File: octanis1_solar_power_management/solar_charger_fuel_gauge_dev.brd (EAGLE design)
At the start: 95 x 43.4 mm, 98 parts, among them IC401 TUSB2046BIRHBIRHB, Q2 32.768kHz, Q4 CSTCR4M00G15L99, Q401 CSTCR6M00G15L99, T1 BC547, U1 BQ24210, U2 BQ27510_DRZ_12, U3 TPS61240DRVT, U402 TPS62237DRY, U404 TPD2E001DRLR, U6 MSP430F5529IPNR

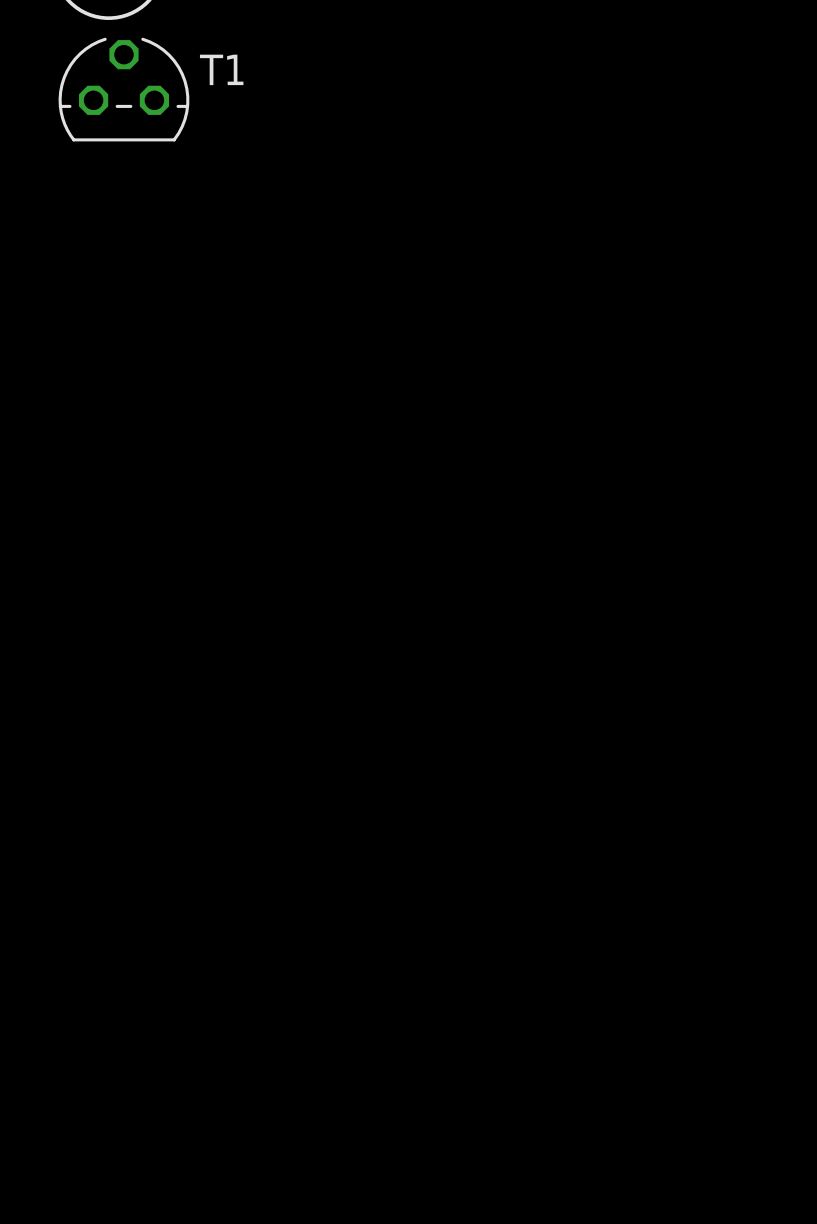
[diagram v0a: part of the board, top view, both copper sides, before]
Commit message: added heating circuit
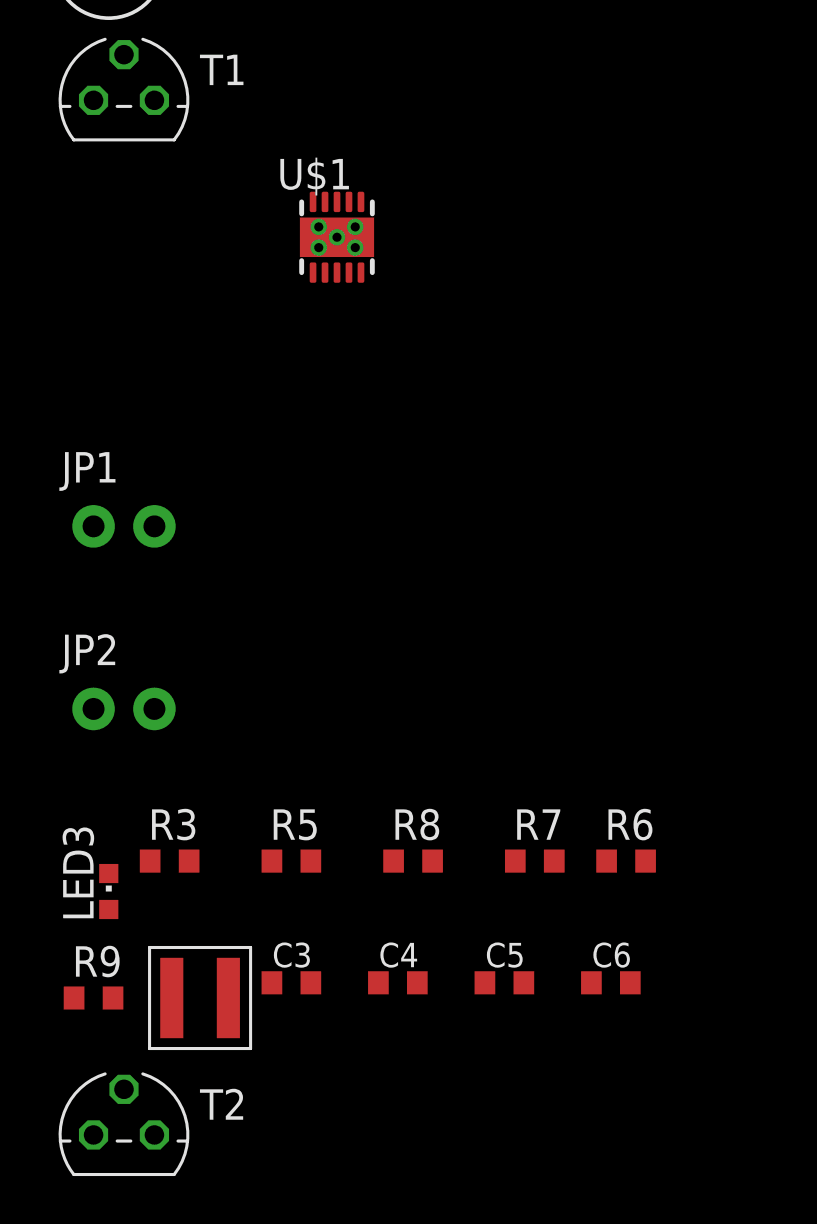
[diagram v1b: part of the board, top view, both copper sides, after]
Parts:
- added C3, C5, C6: 22uF, adafruit:C0603K
- added C4: 10nF, adafruit:C0603K
- added JP1, JP2: M021X02_NO_SILK, SparkFun-Connectors:1X02_NO_SILK
- added L1: 1uH, Coilcraft:XFL4020
- added LED3: (no value), adafruit:CHIPLED_0603
- added R3: 402k, adafruit:R0603
- added R5: 100k, adafruit:R0603
- added R6: 1k, adafruit:R0603
- added R7: 1M, adafruit:R0603
- added R8: 499k, adafruit:R0603
- added R9: 0, adafruit:R0603
- added T2: BC547, transistor:TO92
- added U$1: TPS61230, texas:DRC-S-PVSON-N11
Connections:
- removed net +3V3: C14.1, C19.2, C30.+, HEAT-PAD.2, R27.2, R28.2, RPUC.2, RPUD.2, S5.1, U6.18, U6.50
- removed net N$13: C1.1, SOLAR.2, U1.1
- removed net N$39: T1.1
- removed net N$40: T1.2
- removed net SOLAR: C1.2, R4.1, SOLAR.1, U1.3
- new net IND: L1.P$2, U$1.1, U$1.2
- new net N$42: C4.1, U$1.6
- new net N$43: R3.1, R5.2, U$1.7
- new net N$44: LED3.C, R6.2
- new net N$45: U$1.9
- new net N$46: R8.1, R9.2, U$1.8
- new net N$47: R7.1, R8.2
- new net PG: U$1.5
- new net SOLAR+: C1.1, C14.1, C19.2, C30.+, R27.2, R28.2, RPUC.2, RPUD.2, S5.1, SOLAR.2, T1.3, U1.1, U6.18, U6.50
- new net VIN: C3.1, L1.P$1, R7.2, U$1.10
- new net VOUT: C5.1, C6.1, JP1.1, JP2.1, LED3.A, R3.2, U$1.3, U$1.4
- net BAT+: now also T2.3
- net GND: now also C1.2, C3.2, C4.2, C5.2, C6.2, HEAT-PAD.1, JP1.2, JP2.2, R4.1, R5.1, R6.1, R9.1, SOLAR.1, U$1.GND, U$1.GND@1, U$1.GND@2, U$1.GND@3, U$1.GND@4, U$1.GND@5, U1.3
- net N$37: now also HEAT-PAD.2, T1.1, T2.1; no longer HEAT-PAD.1, T1.3
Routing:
- net SOLAR+: track 0.00 -> 29.0 mm
- net N$13: track 29.0 -> 0.00 mm
- net GND: track 11.7 -> 38.4 mm, vias 0 -> 1
- net SOLAR: track 26.7 -> 0.00 mm, vias 1 -> 0

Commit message: added heating circuit. added correct step up converter. rearranged components to top layer. drew bigger power traces.
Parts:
- removed CPIN: 2.2uF, rcl:C0805
- removed CPOUT: 4.7uF, rcl:C0805
- removed HEAT-PAD: (no value), resistor:P0613V
- removed JP1, JP2: M021X02_NO_SILK, SparkFun-Connectors:1X02_NO_SILK
- removed LP: 1uH, eagle-ltspice:L2012C
- removed R7: 1M, adafruit:R0603
- removed R8: 499k, adafruit:R0603
- removed R9: 0, adafruit:R0603
- removed U3: TPS61240DRVT, TPS61240DRVT:SON65P200X200X80-7N
- added HEATPAD: 22-23-2021, con-molex:22-23-2021
- moved C3 200.3 mm to (19.4, 12.8), turned to 90 degrees
- moved C4 199.6 mm to (23.2, 12.1)
- moved T2 197.1 mm to (13.3, 3.17), turned to 270 degrees
- moved L1 196.8 mm to (16.5, 8.54), turned to 270 degrees
- moved C6 194.4 mm to (28.6, 6.99)
- moved LED3 194.2 mm to (28.6, 8.89), turned to 270 degrees
- moved R6 193.7 mm to (28.6, 11.4)
- moved C5 192.6 mm to (28.6, 5.08)
- moved R5 192.3 mm to (24.8, 9.53), turned to 180 degrees
- moved R3 190.3 mm to (24.8, 6.99)
- moved U$1 164.8 mm to (21.0, 8.35)
- moved T1 159.2 mm to (10.3, 8.57), turned to 270 degrees
- moved U6 14.1 mm to (40.6, 28.0)
- moved TEMP2 12.9 mm to (3.61, 39.4)
- moved RG2 9.93 mm to (4.29, 31.8), turned to 180 degrees
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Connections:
- removed net N$41: LP.2, U3.5
- removed net N$45: U$1.9
- removed net N$46: R8.1, R9.2, U$1.8
- removed net N$47: R7.1, R8.2
- removed net VIN: C3.1, L1.P$1, R7.2, U$1.10
- removed net VOUT: C5.1, C6.1, JP1.1, JP2.1, LED3.A, R3.2, U$1.3, U$1.4
- new net EN_BAT_HEAT: T2.2
- new net EN_SOLAR_HEAT: T1.2
- net 5V: now also C5.1, C6.1, LED3.A, R3.2, U$1.3, U$1.4; no longer CPOUT.1, U3.2, U3.3
- net BAT+: now also C3.1, L1.P$1, U$1.10; no longer CPIN.1, LP.1, U3.6
- net EN5V: now also U$1.9; no longer U3.4
- net GND: now also HEATPAD.2; no longer CPIN.2, CPOUT.2, HEAT-PAD.1, JP1.2, JP2.2, R9.1, U3.1
- net N$37: now also HEATPAD.1; no longer HEAT-PAD.2
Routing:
- net BAT+: track 18.6 -> 72.0 mm
- net SOLAR+: track 29.0 -> 46.6 mm
- net N$37: track 0.00 -> 13.7 mm
- net BAT-: track 3.84 -> 9.46 mm
- net IND: track 0.00 -> 4.60 mm
- net GND: track 38.4 -> 34.7 mm
- added copper zone on layer 16, net GND
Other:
- board size 95 x 43.4 mm -> 75 x 47.4 mm

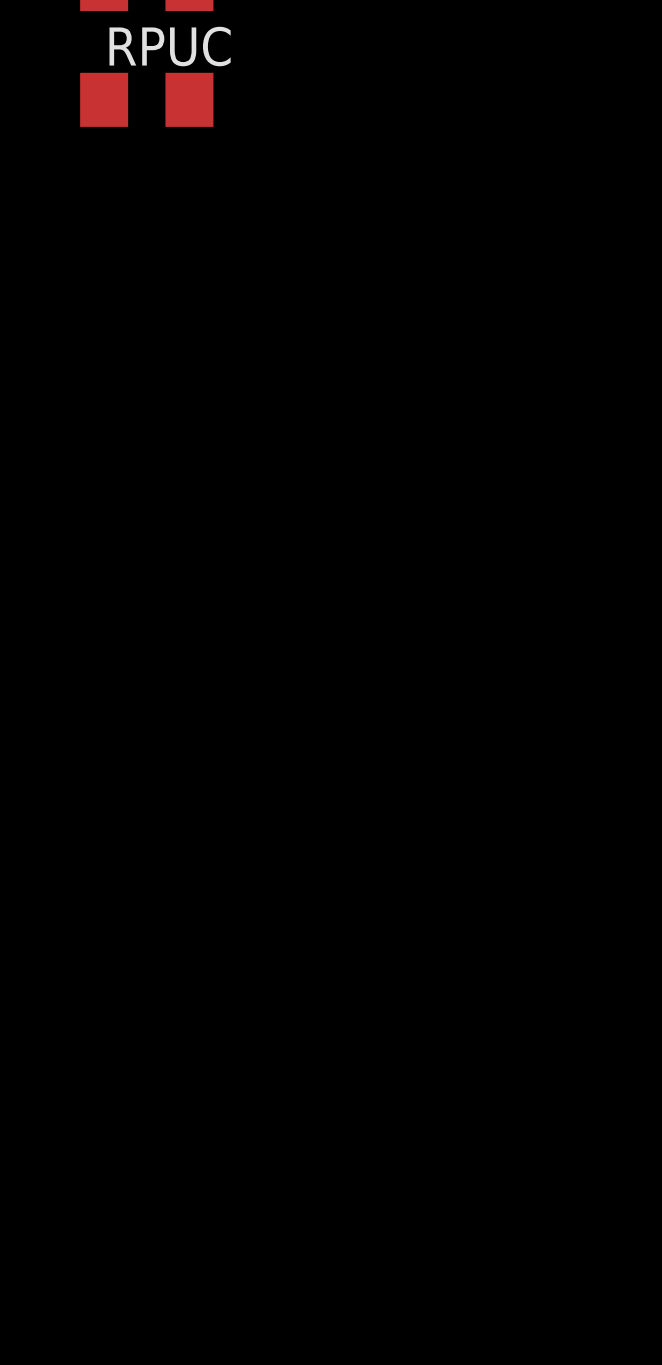
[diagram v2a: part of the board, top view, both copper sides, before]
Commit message: added H-bridge library
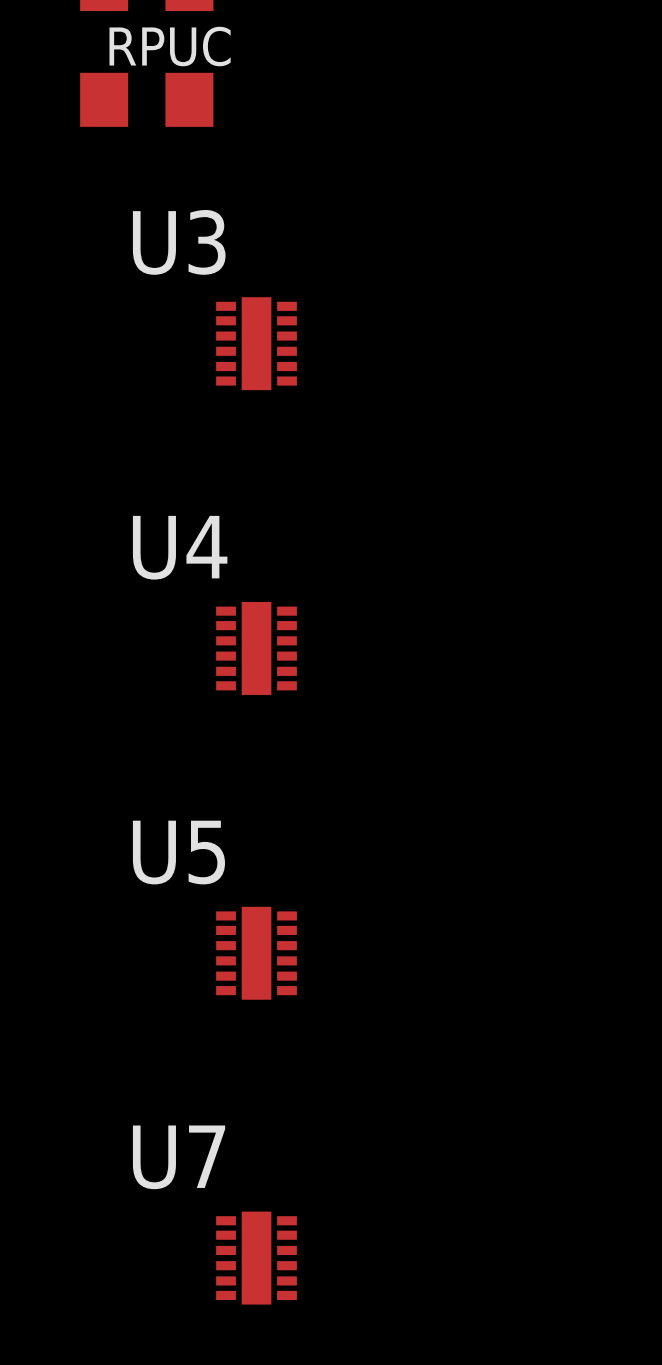
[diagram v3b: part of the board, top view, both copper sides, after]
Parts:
- added U3, U4, U5, U7: DRV8836DSSR, DRV8834:SON50P200X300X80-13N
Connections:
- net BAT+: now also U3.1, U4.1, U5.1, U7.1
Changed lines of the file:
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@@
 <attribute name="OC_FARNELL" value="1462926" x="5.08" y="5.715" size="1.778" layer="27" rot="R90" display="off"/>
+</element>
+<element name="U3" library="DRV8834" package="SON50P200X300X80-13N" value="DRV8836DSSR" x="6.2992" y="-146.9136">
+<attribute name="PACKAGE" value="SON-12" x="6.2992" y="-146.9136" size="1.778" layer="27" display="off"/>
+<attribute name="OC_NEWARK" value="94T6066" x="6.2992" y="-146.9136" size="1.778" layer="27" display="off"/>
+<attribute name="MPN" value="DRV8836DSSR " x="6.2992" y="-146.9136" size="1.778" layer="27" display="off"/>
+<attribute name="SUPPLIER" value="TEXAS INSTRUMENTS" x="6.2992" y="-146.9136" size="1.778" layer="27" display="off"/>
+<attribute name="OC_FARNELL" value="2115236 " x="6.2992" y="-146.9136" size="1.778" layer="27" display="off"/>
+</element>
+<element name="U4" library="DRV8834" package="SON50P200X300X80-13N" value="DRV8836DSSR" x="6.2992" y="-157.0736">
+<attribute name="PACKAGE" value="SON-12" x="6.2992" y="-157.0736" size="1.778" layer="27" display="off"/>
+<attribute name="OC_NEWARK" value="94T6066" x="6.2992" y="-157.0736" size="1.778" layer="27" display="off"/>
+<attribute name="MPN" value="DRV8836DSSR " x="6.2992" y="-157.0736" size="1.778" layer="27" display="off"/>
+<attribute name="SUPPLIER" value="TEXAS INSTRUMENTS" x="6.2992" y="-157.0736" size="1.778" layer="27" display="off"/>
+<attribute name="OC_FARNELL" value="2115236 " x="6.2992" y="-157.0736" size="1.778" layer="27" display="off"/>
+</element>
+<element name="U5" library="DRV8834" package="SON50P200X300X80-13N" value="DRV8836DSSR" x="6.2992" y="-167.2336">
+<attribute name="PACKAGE" value="SON-12" x="6.2992" y="-167.2336" size="1.778" layer="27" display="off"/>
+<attribute name="OC_NEWARK" value="94T6066" x="6.2992" y="-167.2336" size="1.778" layer="27" display="off"/>
+<attribute name="MPN" value="DRV8836DSSR " x="6.2992" y="-167.2336" size="1.778" layer="27" display="off"/>
+<attribute name="SUPPLIER" value="TEXAS INSTRUMENTS" x="6.2992" y="-167.2336" size="1.778" layer="27" display="off"/>
+<attribute name="OC_FARNELL" value="2115236 " x="6.2992" y="-167.2336" size="1.778" layer="27" display="off"/>
+</element>
+<element name="U7" library="DRV8834" package="SON50P200X300X80-13N" value="DRV8836DSSR" x="6.2992" y="-177.3936">
+<attribute name="PACKAGE" value="SON-12" x="6.2992" y="-177.3936" size="1.778" layer="27" display="off"/>
+<attribute name="OC_NEWARK" value="94T6066" x="6.2992" y="-177.3936" size="1.778" layer="27" display="off"/>
+<attribute name="MPN" value="DRV8836DSSR " x="6.2992" y="-177.3936" size="1.778" layer="27" display="off"/>
+<attribute name="SUPPLIER" value="TEXAS INSTRUMENTS" x="6.2992" y="-177.3936" size="1.778" layer="27" display="off"/>
+<attribute name="OC_FARNELL" value="2115236 " x="6.2992" y="-177.3936" size="1.778" layer="27" display="off"/>
 </element>
 </elements>
@@
 <wire x1="19.304" y1="11.8712" x2="19.304" y2="10.16" width="1.016" layer="1"/>
 <wire x1="19.304" y1="10.16" x2="19.1008" y2="10.16" width="1.016" layer="1"/>
-<wire x1="15.367" y1="34.3276" x2="15.367" y2="34.734" width="0" layer="19" extent="1-1"/>
-<wire x1="12.195" y1="34.29" x2="15.367" y2="34.3276" width="0" layer="19" extent="1-1"/>
-<wire x1="10.453" y1="28.9678" x2="12.195" y2="34.29" width="0" layer="19" extent="1-16"/>
+<contactref element="U3" pad="1"/>
+<contactref element="U4" pad="1"/>
+<contactref element="U5" pad="1"/>
+<contactref element="U7" pad="1"/>
+<wire x1="5.2832" y1="-165.989" x2="5.2832" y2="-176.149" width="0" layer="19" extent="1-1"/>
+<wire x1="5.2832" y1="-155.829" x2="5.2832" y2="-165.989" width="0" layer="19" extent="1-1"/>
+<wire x1="5.2832" y1="-145.669" x2="5.2832" y2="-155.829" width="0" layer="19" extent="1-1"/>
+<wire x1="13.335" y1="4.445" x2="5.2832" y2="-145.669" width="0" layer="19" extent="1-1"/>
 <wire x1="10.795" y1="22.6178" x2="12.3952" y2="24.7904" width="0" layer="19" extent="1-16"/>
+<wire x1="12.195" y1="34.29" x2="10.453" y2="28.9678" width="0" layer="19" extent="1-16"/>
+<wire x1="15.367" y1="34.3276" x2="12.195" y2="34.29" width="0" layer="19" extent="1-1"/>
+<wire x1="15.367" y1="34.734" x2="15.367" y2="34.3276" width="0" layer="19" extent="1-1"/>
 </signal>
 <signal name="N$2">
